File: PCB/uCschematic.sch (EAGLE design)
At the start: 62 parts, among them IC1 PIC24FJXXGA002/SO, IC10 ULN2003D1013TR, IC11 ULN2003D1013TR, IC12 ULN2003D1013TR, IC13 FT230XS-U, IC2 317EMP, IC3 MC74HC175ADG, IC4 MC74HC175ADG, IC5 MC74HC175ADG, IC6 MC74HC175ADG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

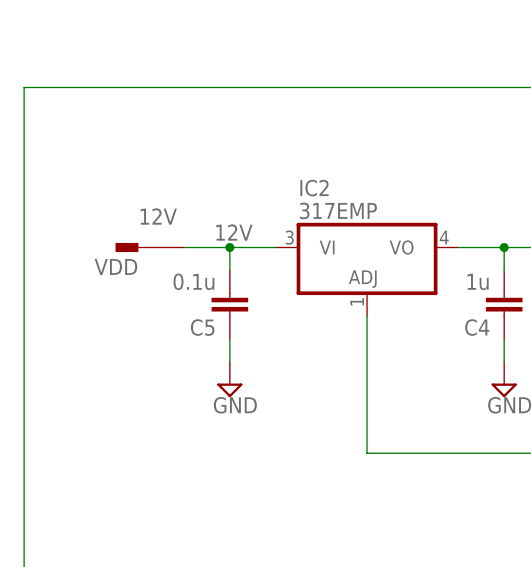
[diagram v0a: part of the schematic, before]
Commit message: Dodan kondenzator većeg kapaciteta na ulazu za napajanje
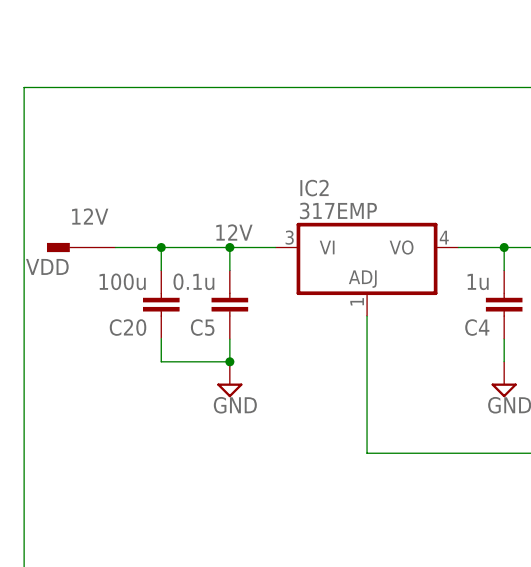
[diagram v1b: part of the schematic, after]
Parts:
- added C20: 100u, eagle-ltspice:C
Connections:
- net 12V: now also C20.2
- net GND: now also C20.1
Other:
- moved on the sheet: VDD
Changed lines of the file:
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@@
 <part name="PGEC_GP" library="5-146280-3" deviceset="5-146280-3" device=""/>
 <part name="PROG_VDD" library="5-146280-3" deviceset="5-146280-3" device=""/>
+<part name="C20" library="eagle-ltspice" library_urn="urn:adsk.eagle:library:217" deviceset="C" device="" package3d_urn="urn:adsk.eagle:package:13265/1" value="100u"/>
 </parts>
 <sheets>
@@
 <attribute name="VALUE" x="-40.005" y="40.005" size="1.778" layer="96"/>
 </instance>
-<instance part="VDD" gate="G$1" x="-48.26" y="58.42" smashed="yes" rot="R180">
-<attribute name="NAME" x="-48.26" y="57.15" size="1.778" layer="95" rot="R180"/>
-<attribute name="VALUE" x="-48.26" y="60.96" size="1.778" layer="96"/>
+<instance part="VDD" gate="G$1" x="-55.88" y="58.42" smashed="yes" rot="R180">
+<attribute name="NAME" x="-55.88" y="57.15" size="1.778" layer="95" rot="R180"/>
+<attribute name="VALUE" x="-55.88" y="60.96" size="1.778" layer="96"/>
 </instance>
 <instance part="SUPPLY1" gate="GND" x="17.78" y="15.24" smashed="yes">
@@
 <attribute name="NAME" x="52.07" y="-91.44" size="1.778" layer="95" rot="R180" align="center-left"/>
 <attribute name="VALUE" x="52.07" y="-88.9" size="1.778" layer="96" rot="R180" align="center-left"/>
+</instance>
+<instance part="C20" gate="G$1" x="-45.72" y="50.8" smashed="yes" rot="R180">
+<attribute name="NAME" x="-47.244" y="50.419" size="1.778" layer="95" rot="R180"/>
+<attribute name="VALUE" x="-47.244" y="55.499" size="1.778" layer="96" rot="R180"/>
 </instance>
 </instances>
@@
 <pinref part="C5" gate="G$1" pin="1"/>
 <wire x1="-38.1" y1="45.72" x2="-38.1" y2="48.26" width="0.1524" layer="91"/>
+<pinref part="C20" gate="G$1" pin="1"/>
+<wire x1="-45.72" y1="48.26" x2="-45.72" y2="45.72" width="0.1524" layer="91"/>
+<wire x1="-45.72" y1="45.72" x2="-38.1" y2="45.72" width="0.1524" layer="91"/>
+<junction x="-38.1" y="45.72"/>
 </segment>
 <segment>
@@
 <wire x1="-38.1" y1="58.42" x2="-38.1" y2="55.88" width="0.1524" layer="91"/>
 <pinref part="VDD" gate="G$1" pin="1"/>
-<wire x1="-38.1" y1="58.42" x2="-43.18" y2="58.42" width="0.1524" layer="91"/>
+<wire x1="-38.1" y1="58.42" x2="-45.72" y2="58.42" width="0.1524" layer="91"/>
 <junction x="-38.1" y="58.42"/>
 <label x="-35.56" y="60.96" size="1.778" layer="95" rot="R180"/>
-</segment>
-<segment>
+<pinref part="C20" gate="G$1" pin="2"/>
+<wire x1="-45.72" y1="58.42" x2="-50.8" y2="58.42" width="0.1524" layer="91"/>
+<wire x1="-45.72" y1="55.88" x2="-45.72" y2="58.42" width="0.1524" layer="91"/>
+<junction x="-45.72" y="58.42"/>
+</segment>
+<segment>
